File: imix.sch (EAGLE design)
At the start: 153 parts, among them Q2 AO3415, Q3 AO3415, Q4 AO3415, Q5 AO3415, U1 BQ2423X, U10 ISL29035, U11 FX0S8700CQ, U12 296-12686-1-ND, U3 TLV3202, U4 LM358, U5 LDO-TPS78233, U6 ATSAM4LCX_100, U8 SI7021, U9 NRF51822, X1 16MHz, X2 16MHz, X3 16MHz

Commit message: Update repo with revision 1.1 and 1.2
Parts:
- removed C30: 100nF, rcl:C-EUC0603
- removed D8: 1N4148XTPMSCT-ND, SparkFun-DiscreteSemi:DIODESOD523
- removed LED1: !CHG, SparkFun-LED:LED-BLUE0603
- removed R19: 1K, SparkFun-Passives:RESISTOR0603-RES
- removed R27, R31, R32: 10K, SparkFun-Passives:RESISTOR0603-RES
- added C8: 4.7uF, rcl:C-EUC0603
- added R4, R5, R6, R7: 10K, SparkFun-Passives:RESISTOR0603-RES
- JP4: value ARDUINO_R3 -> ARDUINO_R3NO_HOLES; device SparkFun-Boards:ARDUINO_R3 -> imix:ARDUINO_R3NO_HOLES
- R16: value 1K -> 10K
- R18: value 1K -> DNP
- R3, R33: value 10K -> 100K
- USB1, USB2: device SparkFun-Connectors:USB-AB -> SparkFun-Connectors-Fixed:USB-AB
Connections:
- removed net N$48: LED1.C, U1.!CHG
- removed net N$50: LED1.A, R19.2
- removed net N$8: C30.1, D8.A, R31.1, R33.1, RESET.3, RESET.4
- net !NRF_PWR_EN: now also R5.2
- net !RESET: now also R33.1, RESET.3, RESET.4; no longer D8.C, R31.2
- net !RF233_PWR_EN: now also R6.2
- net !SENSE_PWR_EN: now also R4.2
- net !TRNG_PWR_EN: now also R7.2
- net GND: now also C8.2, R6.1; no longer C30.2
- net SWDCLK/TCK: no longer R32.1
- net SWDIO/TMS: no longer R27.1
- net VCC_3V3: now also R4.1, R5.1, R7.1
- net VCC_LDO: now also C8.1; no longer R19.1
- net VCC_MCU_3V3: no longer R27.2, R32.2
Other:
- moved on the sheet: BAT1, RESET

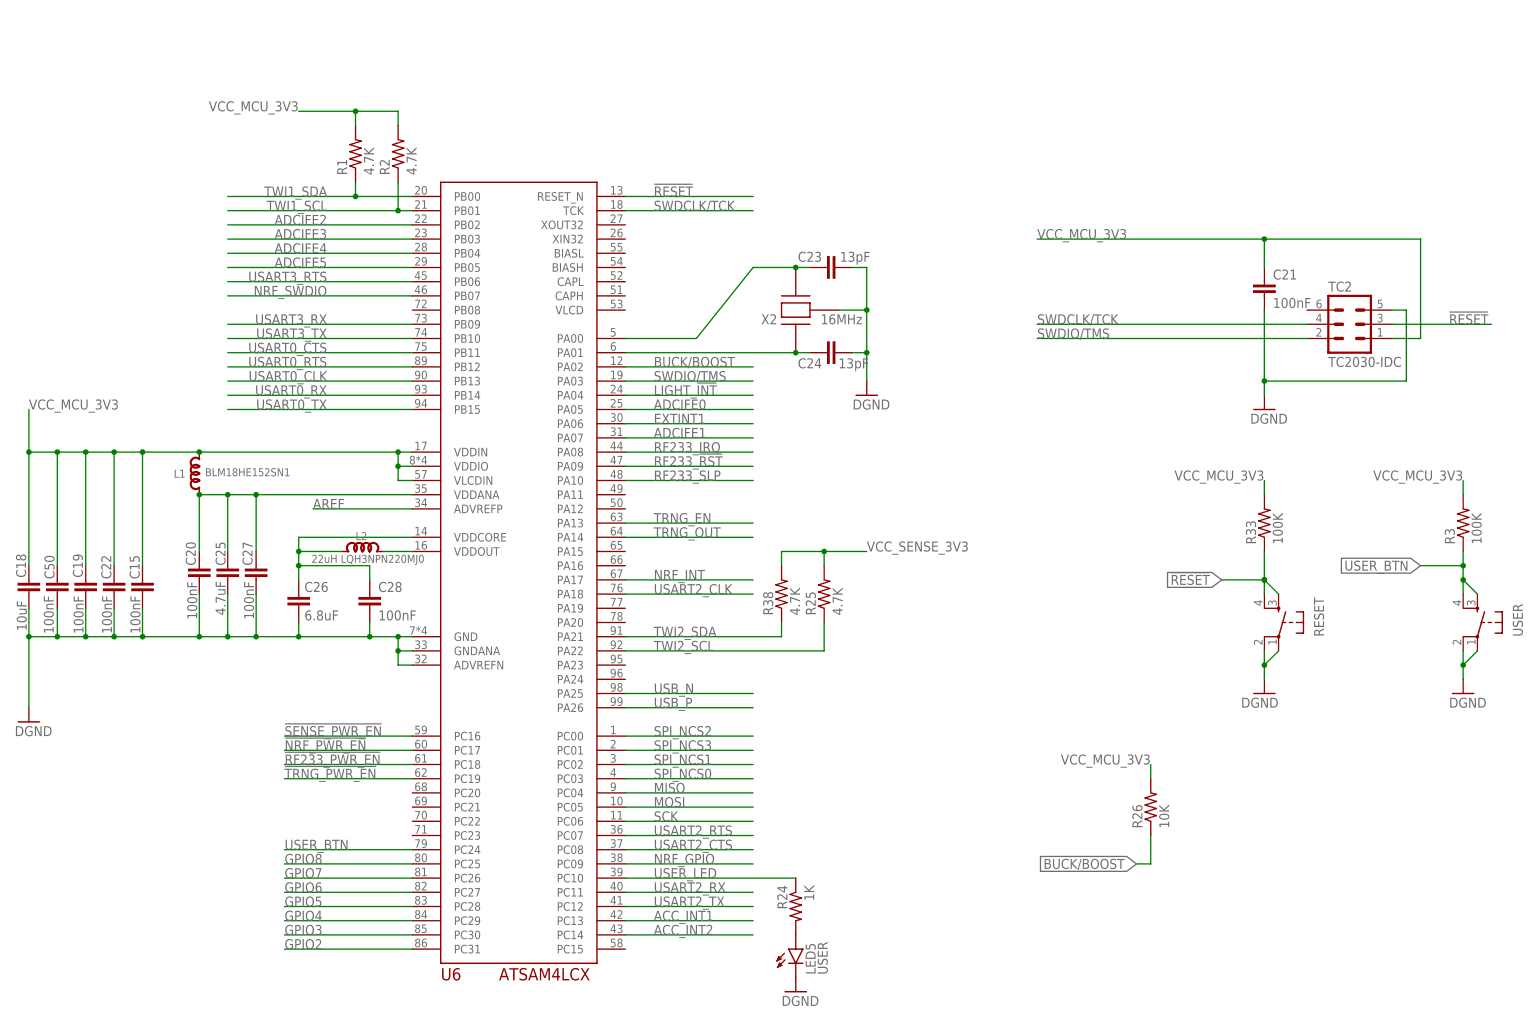
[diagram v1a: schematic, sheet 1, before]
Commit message: Improve schematic readability and update PDF docs: Fixes #10
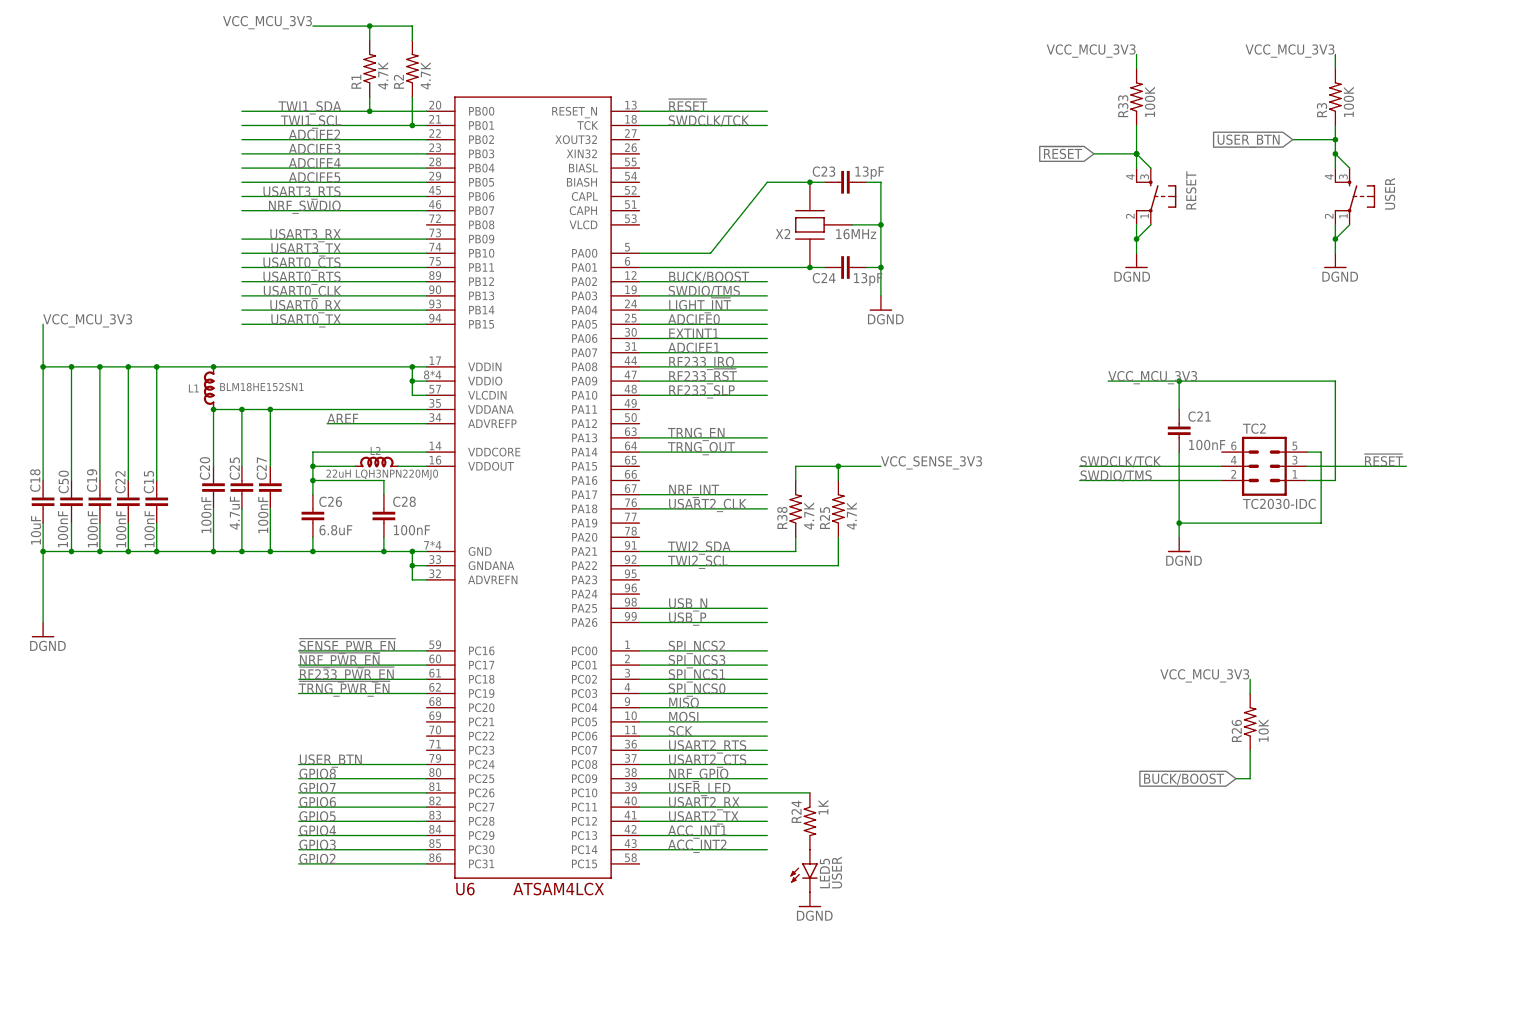
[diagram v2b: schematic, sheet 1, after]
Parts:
- removed JP1, JP3, JP5, JP6, JP8: (no value), SparkFun-Connectors:M02PTH
- removed JP11: (no value), SparkFun-Connectors:M06NO_SILK_FEMALE_PTH
- removed JP15, JP9: (no value), SparkFun-Connectors:M08NO_SILK_FEMALE_PTH
- removed JP2: (no value), SparkFun-Connectors:M10NO_SILK_PTH_FEMALE
- removed JP4: ARDUINO_R3NO_HOLES, imix:ARDUINO_R3NO_HOLES
- removed JP7: (no value), SparkFun-Connectors:M10X2ROUND_NOSILK
- added J1: (no value), SparkFun-Connectors:M10X2ROUND_NOSILK
- added J2: (no value), SparkFun-Connectors:M10NO_SILK_PTH_FEMALE
- added J2_3_5_AND_6: ARDUINO_R3NO_HOLES, imix:ARDUINO_R3NO_HOLES
- added J3, J5: (no value), SparkFun-Connectors:M08NO_SILK_FEMALE_PTH
- added J4.1, J4.2, J4.3, J4.4, J4.5: (no value), SparkFun-Connectors:M02PTH
- added J6: (no value), SparkFun-Connectors:M06NO_SILK_FEMALE_PTH
- C1, C12, C13, C14, C15, C16, C18, C19, C2, C20, C21, C22, C23, C24, C25, C26, C27, C28, C29, C3, C31, C32, C33, C34, C35, C36, C37, C38, C39, C4, C40, C41, C42, C43, C5, C50, C6, C8: device rcl:C-EUC0603 -> imix:C-EUC0603
- C11, C44, C47, C48, C7: device SparkFun-Capacitors:CAP0603-CAP -> imix:C-EUC0603
- C45, C46: device SparkFun-Passives:CAP0603-CAP -> imix:C-EUC0603
- C49: device SparkFun-Capacitors:CAP_POLC -> imix:CAP_POLC
- R1, R16, R17, R18, R2, R20, R21, R22, R23, R24, R25, R26, R28, R29, R3, R33, R34, R35, R36, R37, R38, R4, R5, R6, R7: device SparkFun-Passives:RESISTOR0603-RES -> imix:RESISTOR0603-RES
- R10, R13, R30, R9: device SparkFun-Resistors:RESISTOR0603 -> imix:RESISTOR0603-RES
- R11, R12, R14, R15: device SparkFun-Resistors:0.27OHM-1/10W-1%(0603) -> imix:RESISTOR0603-RES
- U9: value NRF51822 -> NRF51422
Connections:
- net !NRF_PWR_EN: now also J3.7; no longer JP9.7
- net !RESET: now also J1.15, J2_3_5_AND_6.!RESET!@1, J2_3_5_AND_6.!RESET!@2; no longer JP4.!RESET!@1, JP4.!RESET!@2, JP7.15
- net !RF233_PWR_EN: now also J3.6; no longer JP9.6
- net !SENSE_PWR_EN: now also J3.8; no longer JP9.8
- net ACC_INT1: now also J5.1; no longer JP15.1
- net ACC_INT2: now also J6.6; no longer JP11.6
- net ADCIFE0: now also J2_3_5_AND_6.A0; no longer JP4.A0
- net ADCIFE1: now also J2_3_5_AND_6.A1; no longer JP4.A1
- net ADCIFE2: now also J2_3_5_AND_6.A2; no longer JP4.A2
- net ADCIFE3: now also J2_3_5_AND_6.A3; no longer JP4.A3
- net ADCIFE4: now also J2_3_5_AND_6.A4; no longer JP4.A4
- net ADCIFE5: now also J2_3_5_AND_6.A5; no longer JP4.A5
- net AREF: now also J2.3, J2_3_5_AND_6.AREF; no longer JP2.3, JP4.AREF
- net EXTINT1: now also J1.6; no longer JP7.6
- net FTDI0: now also J1.17; no longer JP7.17
- net FTDI1: now also J1.18; no longer JP7.18
- net FTDI2: now also J1.19; no longer JP7.19
- net FTDI3: now also J1.20; no longer JP7.20
- net GND: now also J1.14, J1.16, J2.4, J2_3_5_AND_6.GND, J2_3_5_AND_6.GND@0, J2_3_5_AND_6.GND@1, J2_3_5_AND_6.GND@2, J3.2, J5.7, J5.8; no longer JP15.7, JP15.8, JP2.4, JP4.GND, JP4.GND@0, JP4.GND@1, JP4.GND@2, JP7.14, JP7.16, JP9.2
- net GPIO2: now also J2_3_5_AND_6.D2; no longer JP4.D2
- net GPIO3: now also J2_3_5_AND_6.*D3; no longer JP4.*D3
- net GPIO4: now also J2_3_5_AND_6.D4; no longer JP4.D4
- net GPIO5: now also J2_3_5_AND_6.*D5; no longer JP4.*D5
- net GPIO6: now also J2_3_5_AND_6.*D6; no longer JP4.*D6
- net GPIO7: now also J2_3_5_AND_6.D7; no longer JP4.D7
- net GPIO8: now also J2_3_5_AND_6.D8; no longer JP4.D8
- net LIGHT_!INT: now also J5.6; no longer JP15.6
- net MISO: now also J1.9; no longer JP7.9
- net MOSI: now also J1.11; no longer JP7.11
- net N$14: now also J4.2.1; no longer JP1.1
- net N$18: now also J4.4.1; no longer JP3.1
- net N$36: now also J4.5.1; no longer JP5.1
- net N$37: now also J4.1.1; no longer JP6.1
- net NRF_GPIO: now also J1.12; no longer JP7.12
- net NRF_INT: now also J3.3; no longer JP9.3
- net NRF_SWDIO: now also J6.3; no longer JP11.3
- net RF233_!RST: now also J6.2; no longer JP11.2
- net RF233_IRQ: now also J6.5; no longer JP11.5
- net RF233_SLP: now also J6.1; no longer JP11.1
- net SCK: now also J1.13; no longer JP7.13
- net SPI_NCS0: now also J1.7; no longer JP7.7
- net SPI_NCS1: now also J1.5; no longer JP7.5
- net SPI_NCS2: now also J1.1; no longer JP7.1
- net SPI_NCS3: now also J1.3; no longer JP7.3
- net TRNG_EN: now also J3.5; no longer JP9.5
- net TRNG_OUT: now also J3.4; no longer JP9.4
- net TWI1_SCL: now also J1.4, J2.1, J2_3_5_AND_6.SCL; no longer JP2.1, JP4.SCL, JP7.4
- net TWI1_SDA: now also J1.2, J2.2, J2_3_5_AND_6.SDA; no longer JP2.2, JP4.SDA, JP7.2
- net TWI2_SCL: now also J2.7; no longer JP2.7
- net TWI2_SDA: now also J2.8; no longer JP2.8
- net USART0_CLK: now also J2_3_5_AND_6.D13, J2_3_5_AND_6.SCK; no longer JP4.D13, JP4.SCK
- net USART0_CTS: now also J2_3_5_AND_6.*D9; no longer JP4.*D9
- net USART0_RTS: now also J2_3_5_AND_6.*D10; no longer JP4.*D10
- net USART0_RX: now also J2.5, J2_3_5_AND_6.D12, J2_3_5_AND_6.MISO; no longer JP2.5, JP4.D12, JP4.MISO
- net USART0_TX: now also J2.6, J2_3_5_AND_6.*D11, J2_3_5_AND_6.MOSI; no longer JP2.6, JP4.*D11, JP4.MOSI
- net USART2_CLK: now also J2.9; no longer JP2.9
- net USART2_CTS: now also J5.4; no longer JP15.4
- net USART2_RTS: now also J5.5; no longer JP15.5
- net USART2_RX: now also J5.3; no longer JP15.3
- net USART2_TX: now also J5.2; no longer JP15.2
- net USART3_RTS: now also J6.4; no longer JP11.4
- net USART3_RX: now also J2_3_5_AND_6.D0, J3.1; no longer JP4.D0, JP9.1
- net USART3_TX: now also J2.10, J2_3_5_AND_6.D1; no longer JP2.10, JP4.D1
- net USER_BTN: now also J1.10; no longer JP7.10
- net USER_LED: now also J1.8; no longer JP7.8
- net VCC_3V3: now also J2_3_5_AND_6.3.3V, J2_3_5_AND_6.IOREF, J4.1.2, J4.2.2, J4.3.1, J4.4.2, J4.5.2; no longer JP1.2, JP3.2, JP4.3.3V, JP4.IOREF, JP5.2, JP6.2, JP8.1
- net VCC_EXT_5V: now also J2_3_5_AND_6.5V, J2_3_5_AND_6.VCC, J2_3_5_AND_6.VIN; no longer JP4.5V, JP4.VCC, JP4.VIN
- net VCC_MCU_3V3: now also J4.3.2; no longer JP8.2
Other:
- moved on the sheet: B1, B2, BAT1, C1, C11, C12, C13, C14, C15, C16, C17, C18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
